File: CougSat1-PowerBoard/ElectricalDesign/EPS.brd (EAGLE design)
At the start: 90.4 x 95.8 mm, 416 parts, among them J1 Deployable 0, J2 PV0, J3 PV1, J4 Umbilical, J5 CougSat Card, J6 SWD, J7 PV2, J8 PV3, J9 Deployable 1, Q1 CSD25402Q3A, Q2 DMN2008LFU, Q3 DMN2008LFU, Q4 CSD25402Q3A, Q5 CSD25402Q3A, Q6 DMN53D0LDW, Q7 DMN53D0LDW, Q8 CSD25402Q3A, SW1 ESE24MH1, U1 INA199C1, U10 INA199C2, U11 INA199C1, U12 AD7689, U13 INA199C2, U14 TPS2115A, U15 TXS0102DQM, U16 TXS0102DQM, U17 AD8515, U18 BQ29700, U19 TPS2115A, U2 AD7689, U20 TXS0102DQM, U21 TXS0102DQM, U22 STM32L476RGT, U23 AD7291, U24 TPS2115A, U25 TPS2115A, U26 BQ29700, U27 TPS2115A, U28 TPS2115A, U29 TPS2115A, U3 AD8515, U30 TPS2115A, U31 INA199C1, U32 TPS2115A, U33 TPS2115A, U34 INA199C1, U35 AD7291, U36 TPS2115A, U37 AD7689, U38 TPS2115A, U39 AD7291, U4 TPS2115A, U40 AD8515, U41 TPS2115A, U42 TPS2115A, U43 TPS2115A, U44 INA199C1, U45 TPS2115A, U46 TPS2115A, U47 TPS64200, U48 TPS2115A, U49 TPS2115A, U5 AD7291, U50 AD7291, U51 TPS2115A, U52 TPS2115A, U53 TPS2115A, U54 TPS2115A, U55 TPS2115A, U6 INA199C1, U7 TPS2115A, U8 TXS0102DQM, U9 TPS64200, Y1 8MHz ±10ppm, Y2 32.768kHz ±10ppm

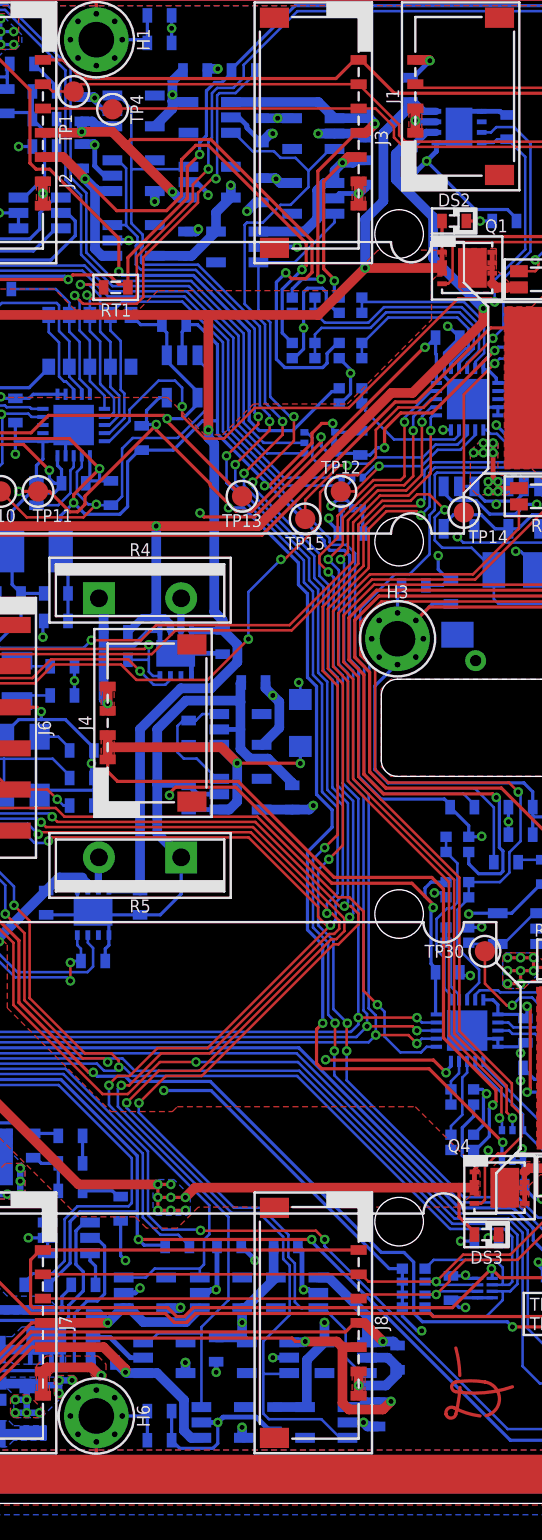
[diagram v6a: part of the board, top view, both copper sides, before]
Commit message: Updated block diagram
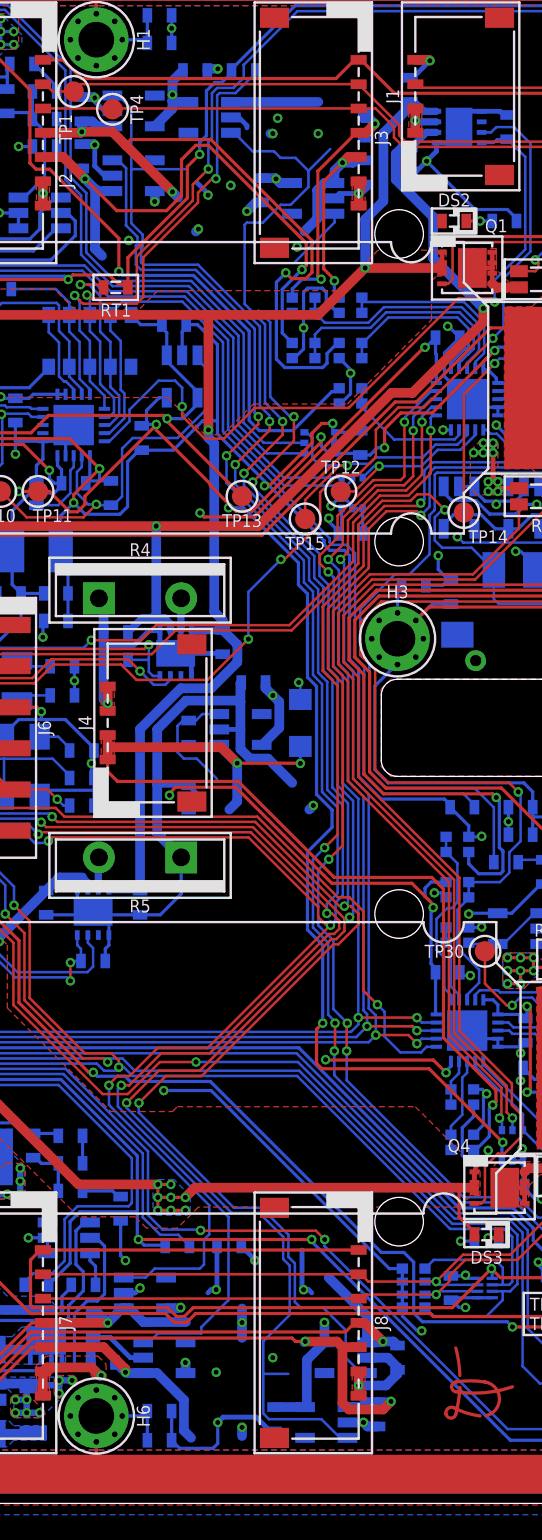
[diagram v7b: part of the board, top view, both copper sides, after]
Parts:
- removed C112, C125, C19, C29, C60: 1µF 10%, CougsInSpace-Capacitors:1608
- removed D10, D15, D16, D19, D2, D21, D4, D7, D8: MAX40200, CougsInSpace-DiscreteSemi:SOT23-5
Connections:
- removed net VIN-A: C117.1, C134.1, C30.1, C6.1, C67.1, D1.5, D11.5, D13.1, D17.5, D20.5, D22.5, D23.5, D3.5, D5.5, D9.5, R2.2
- new net VBATT: DS2.A, Q1.1, Q1.2, Q1.3
- net PC_PV-0/2A: no longer D19.3, D8.3
- net PC_PV-0/2B: no longer D16.3, D2.3
- net PC_PV-1/3A: no longer D21.3, D7.3
- net PC_PV-1/3B: no longer D15.3, D4.3
- net PGND: no longer C112.2, C125.2, C19.2, C29.2, C60.2, D10.2, D15.2, D16.2, D19.2, D2.2, D21.2, D4.2, D7.2, D8.2
- net PV_IN-0A: no longer D19.1
- net PV_IN-0B: no longer D16.1
- net PV_IN-1A: no longer D21.1
- net PV_IN-1B: no longer D15.1
- net PV_IN-2A: no longer D8.1
- net PV_IN-2B: no longer D2.1
- net PV_IN-3A: no longer D7.1
- net PV_IN-3B: no longer D4.1
- net UMB_EN: no longer D10.3
- net UMB_IN: no longer D10.1
- net VBATT-A: no longer DS2.A, Q1.1, Q1.2, Q1.3
- net VIN: now also C117.1, C134.1, C30.1, C6.1, C67.1, D1.5, D11.5, D13.1, D17.5, D20.5, D22.5, D23.5, D3.5, D5.5, D9.5, R2.2
- net VIN-B: no longer C112.1, C125.1, C19.1, C29.1, C60.1, D10.5, D15.5, D16.5, D19.5, D2.5, D21.5, D4.5, D7.5, D8.5
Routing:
- net VIN: track 13.5 -> 159.2 mm, vias 2 -> 19
- net VIN-A: track 145.7 -> 0.00 mm, vias 17 -> 0
- net VIN-B: track 170.7 -> 151.2 mm
- net PGND: track 1160.6 -> 1145.9 mm
- net PC_PV-0/2B: track 128.2 -> 122.9 mm
- net PC_PV-1/3B: track 128.8 -> 123.5 mm
- net VBATT-A: track 315.7 -> 312.5 mm
- net PV_IN-1A: track 23.8 -> 20.6 mm
- net PV_IN-1B: track 20.2 -> 17.4 mm
- net UMB_IN: track 66.5 -> 64.0 mm
- net PC_PV-1/3A: track 132.0 -> 130.3 mm
- net PV_IN-2A: track 38.4 -> 37.2 mm
- net PV_IN-3B: track 55.2 -> 54.2 mm
- net PC_PV-0/2A: track 127.9 -> 127.1 mm
- net VBATT: track 0.00 -> 0.65 mm
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- added copper zone on layer 1, net VIN
- added copper zone on layer 15, net VIN
- added copper zone on layer 16, net VIN
- added copper zone on layer 2, net VIN
- removed copper zone on layer 1, net VIN-A
- removed copper zone on layer 15, net VIN-A
- removed copper zone on layer 16, net VIN-A
- removed copper zone on layer 2, net VIN-A

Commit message: Implement schematic changes
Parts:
- removed C10, C100, C121, C132, C139, C15, C22, C24, C25, C28, C35, C4, C41, C43, C49, C50, C71, C73, C75, C83: 100nF 10%, CougsInSpace-Capacitors:1608
- removed C107, C20: 1µF 10%, CougsInSpace-Capacitors:1608
- removed C11, C26, C3, C31: 10µF 10%, CougsInSpace-Capacitors:3216
- removed C12: 470pF 1%, CougsInSpace-Capacitors:1608
- removed C33: 220µF 10%, CougsInSpace-Capacitors:7132-POL
- removed C34: 4.7pF ±0.1, CougsInSpace-Capacitors:1608
- removed C45: 10µF 10%, CougsInSpace-Capacitors:1608
- removed D12: SS1FH10, CougsInSpace-DiscreteSemi:DO-219AB
- removed D13, D14: MAX40200, CougsInSpace-DiscreteSemi:SOT23-5
- removed D6: MBRM120LT, CougsInSpace-DiscreteSemi:POWERMITE
- removed DS4, DS5: Green, CougsInSpace-LEDs:1608-POL
- removed H5, H6: M2, CougsInSpace-Hardware:MOUNTING_HOLE-2.2
- removed L1: 4.7µH 20%, CougsInSpace-Coils:7575
- removed R36: 10kΩ 0.1%, CougsInSpace-Resistors:1608
- removed RN4: 5kΩ 0.1%, CougsInSpace-Resistors:1616
- removed U52, U53, U54, U55: TPS2115A, CougsInSpace-IC-Power:VSON-8
- added J10: Battery -, CougsInSpace-Connectors:THT-1.5
- added J11: PGND, CougsInSpace-Connectors:THT-1.5
- added J12: Battery +, CougsInSpace-Connectors:THT-1.5
- added J13: VBatt, CougsInSpace-Connectors:THT-1.5
- added Q10, Q12, Q14, Q16, Q17, Q18, Q20, Q21, Q22, Q24, Q26, Q28, Q29, Q30, Q32, Q34, Q35, Q37, Q38, Q40, Q41, Q43, Q9: CSD25402Q3A, CougsInSpace-DiscreteSemi:SON-3333
- added Q11, Q13, Q15, Q19, Q23, Q25, Q27, Q31, Q33, Q36, Q39, Q42: DMN53D0LDW, CougsInSpace-DiscreteSemi:SOT363
- added R84, R86, R88, R90: 12mΩ 1%, CougsInSpace-Resistors:3216-KELVIN
- added R85, R87, R89, R91: 10kΩ 0.1%, CougsInSpace-Resistors:1608
- added RN22, RN23, RN24: 10kΩ 5%, CougsInSpace-Resistors:3264
- added TP44, TP45, TP46, TP47, TP48, TP49, TP50, TP51, TP52, TP53, TP54, TP55, TP56, TP57, TP58, TP59, TP60, TP61, TP62, TP63, TP64: TEST_POINT-SMD-C-1.25, CougsInSpace-Connectors:SMD-C-1.25
- DS1: value Green -> Yellow
- DS3: value Green -> Blue
- Q5: value CSD25402Q3A -> DMN53D0LDW; device CougsInSpace-DiscreteSemi:SON-3333 -> CougsInSpace-DiscreteSemi:SOT363
- Q7: value DMN53D0LDW -> CSD25402Q3A; device CougsInSpace-DiscreteSemi:SOT363 -> CougsInSpace-DiscreteSemi:SON-3333
- R10, R74: value 470Ω 0.5% -> 12mΩ 1%; device CougsInSpace-Resistors:1608 -> CougsInSpace-Resistors:3216-KELVIN
- R11: value 12mΩ 1% -> 10kΩ 0.1%; device CougsInSpace-Resistors:3216-KELVIN -> CougsInSpace-Resistors:1608
- R12, R51, R55, R60, R65, R71, R73, R76, R81: value 2.2kΩ 1% -> 10kΩ 0.1%
- R13: value 150Ω 1% -> 12mΩ 1%; device CougsInSpace-Resistors:1608 -> CougsInSpace-Resistors:3216-KELVIN
- R14: value 10mΩ 1% -> 10kΩ 0.1%; device CougsInSpace-Resistors:3216 -> CougsInSpace-Resistors:1608
- R15, R9: value 0Ω <20mΩ -> 12mΩ 1%; device CougsInSpace-Resistors:1608 -> CougsInSpace-Resistors:3216-KELVIN
- R16, R47, R69: value 1kΩ 0.1% -> 10kΩ 0.1%
- R17: value 1kΩ 0.1% -> 100kΩ 0.1%
- R18: value 360kΩ 1% -> 12mΩ 1%; device CougsInSpace-Resistors:1608 -> CougsInSpace-Resistors:3216-KELVIN
- R19, R21, R23: value 0Ω <20mΩ -> 10kΩ 0.1%
- R20: value 620kΩ 1% -> 12mΩ 1%; device CougsInSpace-Resistors:1608 -> CougsInSpace-Resistors:3216-KELVIN
- R24, R50, R54, R57, R59, R70, R79: value 2.2kΩ 1% -> 12mΩ 1%; device CougsInSpace-Resistors:1608 -> CougsInSpace-Resistors:3216-KELVIN
- R26, R39, R63: value 750Ω 0.5% -> 12mΩ 1%; device CougsInSpace-Resistors:1608 -> CougsInSpace-Resistors:3216-KELVIN
- R38, R45, R58: value 750Ω 0.5% -> 10kΩ 0.1%
- R52: value 10kΩ 0.1% -> 12mΩ 1%; device CougsInSpace-Resistors:1608 -> CougsInSpace-Resistors:3216-KELVIN
- R53: value 536kΩ 1% -> 10kΩ 0.1%
- R56: value 1kΩ 0.1% -> 12mΩ 1%; device CougsInSpace-Resistors:1608 -> CougsInSpace-Resistors:3216-KELVIN
- R67: value 1.2kΩ 0.1% -> 12mΩ 1%; device CougsInSpace-Resistors:1608 -> CougsInSpace-Resistors:3216-KELVIN
- TP37: value TEST_POINT-THT-0.7 -> TEST_POINT-SMD-C-1.25; device CougsInSpace-Connectors:THT-0.7 -> CougsInSpace-Connectors:SMD-C-1.25
- U1, U6: value INA199C1 -> INA199C2
- U14, U19, U24, U25, U27, U28, U29, U30, U32, U33, U36, U38, U4, U41, U42, U43, U45, U46, U48, U49, U51, U7: value TPS2115A -> INA199C2; device CougsInSpace-IC-Power:VSON-8 -> CougsInSpace-IC-Amplifiers:SOT363
- U9: value TPS64200 -> INA199C2; device CougsInSpace-IC-Power:SOT23-6 -> CougsInSpace-IC-Amplifiers:SOT363
- moved DS1 292.1 mm to (-33.2, -245.4)
- moved R81 257.9 mm to (-10.0, -213.6), flipped to the top, turned to 0 degrees
- moved R74 257.0 mm to (-9.20, -202.9), flipped to the top, turned to 0 degrees
- moved R76 254.3 mm to (-12.9, -213.6), flipped to the top, turned to 0 degrees
- moved R79 254.1 mm to (-32.7, -206.8), flipped to the top, turned to 0 degrees
- moved R73 253.9 mm to (-15.8, -213.6), flipped to the top, turned to 0 degrees
- moved R29 238.5 mm to (-33.2, -242.2), flipped to the top, turned to 0 degrees
- moved U51 238.4 mm to (-11.0, -198.9), flipped to the top
- moved R38 234.1 mm to (-27.4, -213.6), flipped to the top, turned to 0 degrees
- moved R55 231.7 mm to (-18.7, -213.6), flipped to the top, turned to 0 degrees
- moved RT5 231.1 mm to (-33.2, -248.6), flipped to the top
- moved R51 228.3 mm to (-21.6, -213.6), flipped to the top, turned to 0 degrees
- moved R69 225.7 mm to (-23.9, -167.8), flipped to the top
- moved R45 224.9 mm to (-24.5, -213.6), flipped to the top, turned to 0 degrees
- moved R56 223.7 mm to (-13.9, -202.9), flipped to the top, turned to 0 degrees
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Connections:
- net 3.3V_I-A renamed 3.3V_I
- net 3.3V_ISENS-A renamed 3.3V_ISENS
- net 3.3V_LED-A renamed 3.3V_LED
- net 3.3V_REG_BUCK_NODE-A renamed 3.3V_REG_BUCK_NODE
- net 3.3V_REG_FB-A renamed 3.3V_REG_FB
- net 3.3V_REG_FBRES_HIGH-A renamed 3.3V_REG_FBRES_HIGH
- net 3.3V_REG_FBRES_LOW-A renamed 3.3V_REG_FBRES_LOW
- net 3.3V_REG_INCAP-A renamed 3.3V_REG_INCAP
- net 3.3V_REG_OUTCAP-A renamed 3.3V_REG_OUTCAP
- net 3.3V_REG_RSENS-A renamed 3.3V_REG_RSENS
- net 3.3V_REG_SNUBBER-A renamed 3.3V_REG_SNUBBER
- net 3.3V_REG_SW-A renamed 3.3V_REG_SW
- net 3.3V_REG_SW_GATE-A renamed 3.3V_REG_SW_GATE
- net I_3.3V_IN-A renamed I_3.3V_IN
- net I_3.3V_IN-A_N renamed I_3.3V_IN_N
- net I_3.3V_IN-A_P renamed I_3.3V_IN_P
- net I_3.3V_OUT-A renamed I_3.3V_OUT
- net I_3.3V_OUT-A_N renamed I_3.3V_OUT_N
- net I_3.3V_OUT-A_P renamed I_3.3V_OUT_P
- net TEMP-REG-A renamed TEMP-REG
- net TEMP-REG-B renamed TEMP-PCB-5
- removed net !PC_DEPLOY-0: U22.9, U52.3
- removed net !PC_DEPLOY-1: U22.25, U4.3
- removed net !VBATT_EN: Q1.4, Q4.4, Q7.2, Q7.3, R52.2
- removed net 3.3V-A: C100.1, C24.1, C41.1, DS1.A, R82.2, RN16.2, U14.8, U36.8, U38.8, U41.8, U42.8, U43.8, U45.8, U46.8, U48.8, U49.8, U51.8, U53.8, U54.8, U55.8, U7.8
- removed net 3.3V-B: C139.1, C28.1, C43.1, DS4.A, R22.1, RN4.2, U14.6, U36.6, U38.6, U41.6, U42.6, U43.6, U45.6, U46.6, U48.6, U49.6, U51.6, U53.6, U54.6, U55.6, U7.6
- removed net 3.3V_I-B: C31.1, C33.A, C34.1, L1.2, R22.2, R23.2, TP36.1
- removed net 3.3V_ISENS-B: Q5.5, Q5.6, Q5.7, Q5.8, Q5.PAD, R14.1, U9.4
- removed net 3.3V_LED-B: DS4.C, R16.2
- removed net 3.3V_REG_BUCK_NODE-B: D6.C, L1.1, Q5.1, Q5.2, Q5.3, R13.2
- removed net 3.3V_REG_FB-B: C34.2, R19.2, R20.1, U9.3
- removed net 3.3V_REG_FBRES_HIGH-B: R20.2, R23.1
- removed net 3.3V_REG_FBRES_LOW-B: R18.2, R19.1
- removed net 3.3V_REG_INCAP-B: C11.2, C3.1
- removed net 3.3V_REG_OUTCAP-B: C26.1, C31.2
- removed net 3.3V_REG_RSENS-B: R11.1, R14.2
- removed net 3.3V_REG_SNUBBER-B: C12.1, R13.1
- removed net 3.3V_REG_SW-B: R15.1, U9.6
- removed net 3.3V_REG_SW_GATE-B: Q5.4, R15.2
- removed net ADC_3.3V-B: RN4.3, RN4.4, U2.6
- removed net EJECT_TIMER_DISCHARGE: Q7.6, R33.1
- removed net I_3.3V: R24.2, U14.4, U23.4
- removed net I_3.3V_IN-B: TP43.1, U1.6, U2.8
- removed net I_3.3V_IN-B_N: R11.1-KELVIN, U1.5
- removed net I_3.3V_IN-B_P: R11.2-KELVIN, U1.4
- removed net I_3.3V_OUT-B: TP42.1, U2.7, U6.6
- removed net I_3.3V_OUT-B_N: R22.1-KELVIN, U6.5
- removed net I_3.3V_OUT-B_P: R22.2-KELVIN, U6.4
- removed net I_DEPLOY-0: R74.2, U35.5, U52.4
- removed net I_DEPLOY-1: R10.2, U4.4, U5.18
- removed net PC_PV-0/2A: D23.3, D9.3, U22.16
- removed net PC_PV-0/2B: D20.3, D5.3, U22.15
- removed net PC_PV-1/3A: D22.3, D3.3, U22.11
- removed net PC_PV-1/3B: D1.3, D17.3, U22.14
- removed net PR_DEPLOY-0: J1.1, J1.2, U52.7
- removed net PR_DEPLOY-1: J9.1, J9.2, U4.7
- removed net PWR_CTRL_SW: J5.A40, J5.B40, R47.1, SW1.1, SW1.2
- removed net UMB_EN: D11.3, R36.1
- removed net VBATT_EN: D12.C, Q7.5, R47.2, R53.1
- removed net VBATT_LED-A: DS2.C, R69.2
- removed net VBATT_LED-B: DS3.C, R17.2
- removed net VIN-B: D14.1, R7.1
- removed net VIN_BATT-A: BT1.C, R1.2, R2.1, R37.2
- removed net VIN_BATT-B: BT2.C, R27.2, R7.2, R8.1
- removed net VIN_OUT-A: Q1.5, Q1.6, Q1.7, Q1.8, Q1.PAD, R1.1
- removed net VIN_OUT-B: Q4.5, Q4.6, Q4.7, Q4.8, Q4.PAD, R8.2
- new net !PC_DP-0: Q39.3, Q40.4, R87.1
- new net !PC_DP-1: Q41.4, Q42.6, R89.1
- new net BATTERY+: J12.1, R1.1, R8.2
- new net BATTERY-: J10.1, Q2.1, Q3.6, R30.1, R31.1, R41.1, R46.1, TP17.1, TP19.1
- new net CHASSIS_REG1: C136.1, H1.1, H1.V1, H1.V2, H1.V3, H1.V4, H1.V5, H1.V6, H1.V7, H1.V8, R83.2
- new net CHASSIS_REG2: C109.1, H2.1, H2.V1, H2.V2, H2.V3, H2.V4, H2.V5, H2.V6, H2.V7, H2.V8, R62.2
- new net I_3.3V-0_N: R9.1-KELVIN, U1.5
- new net I_3.3V-0_P: R9.2-KELVIN, U1.4
- new net I_3.3V-10_N: R63.1-KELVIN, U46.5
- new net I_3.3V-10_P: R63.2-KELVIN, U46.4
- new net I_3.3V-11_N: R67.1-KELVIN, U48.5
- new net I_3.3V-11_P: R67.2-KELVIN, U48.4
- new net I_3.3V-12_N: R70.1-KELVIN, U49.5
- new net I_3.3V-12_P: R70.2-KELVIN, U49.4
- new net I_3.3V-1_N: R13.1-KELVIN, U6.5
- new net I_3.3V-1_P: R13.2-KELVIN, U6.4
- new net I_3.3V-2_N: R15.1-KELVIN, U9.5
- new net I_3.3V-2_P: R15.2-KELVIN, U9.4
- new net I_3.3V-3_N: R18.1-KELVIN, U14.5
- new net I_3.3V-3_P: R18.2-KELVIN, U14.4
- new net I_3.3V-4_N: R20.1-KELVIN, U36.5
- new net I_3.3V-4_P: R20.2-KELVIN, U36.4
- new net I_3.3V-5_N: R22.1-KELVIN, U38.5
- new net I_3.3V-5_P: R22.2-KELVIN, U38.4
- new net I_3.3V-6_N: R24.1-KELVIN, U41.5
- new net I_3.3V-6_P: R24.2-KELVIN, U41.4
- new net I_3.3V-7_N: R52.1-KELVIN, U42.5
- new net I_3.3V-7_P: R52.2-KELVIN, U42.4
- new net I_3.3V-8_N: R57.1-KELVIN, U43.5
- new net I_3.3V-8_P: R57.2-KELVIN, U43.4
- new net I_3.3V-9_N: R59.1-KELVIN, U45.5
- new net I_3.3V-9_P: R59.2-KELVIN, U45.4
- new net I_3.3V-PV_N: R90.1-KELVIN, U51.5
- new net I_3.3V-PV_P: R90.2-KELVIN, U51.4
- new net I_BATT-0_N: R10.1-KELVIN, U4.5
- new net I_BATT-0_P: R10.2-KELVIN, U4.4
- new net I_BATT-1_N: R26.1-KELVIN, U7.5
- new net I_BATT-1_P: R26.2-KELVIN, U7.4
- new net I_BATT-2_N: R39.1-KELVIN, U19.5
- new net I_BATT-2_P: R39.2-KELVIN, U19.4
- new net I_BATT-3_N: R50.1-KELVIN, U24.5
- new net I_BATT-3_P: R50.2-KELVIN, U24.4
- new net I_BATT-4_N: R54.1-KELVIN, U25.5
- new net I_BATT-4_P: R54.2-KELVIN, U25.4
- new net I_BATT-5_N: R56.1-KELVIN, U27.5
- new net I_BATT-5_P: R56.2-KELVIN, U27.4
- new net I_BATT-6_N: R74.1-KELVIN, U28.5
- new net I_BATT-6_P: R74.2-KELVIN, U28.4
- new net I_BH-0_N: R79.1-KELVIN, U29.5
- new net I_BH-0_P: R79.2-KELVIN, U29.4
- new net I_BH-1_N: R84.1-KELVIN, U30.5
- new net I_BH-1_P: R84.2-KELVIN, U30.4
- new net I_DP-0: TP62.1, U32.6, U35.5
- new net I_DP-0_N: R86.1-KELVIN, U32.5
- new net I_DP-0_P: R86.2-KELVIN, U32.4
- new net I_DP-1: TP63.1, U33.6, U5.18
- new net I_DP-1_N: R88.1-KELVIN, U33.5
- new net I_DP-1_P: R88.2-KELVIN, U33.4
- new net PC_3.3V-0: Q5.2, RN22.1, U22.57
- new net PC_3.3V-1: Q5.5, RN22.9, U22.56
- new net PC_3.3V-10: Q27.2, RN23.2, U22.41
- new net PC_3.3V-11: Q27.5, RN23.8, U22.39
- new net PC_3.3V-12: Q31.2, RN23.3, U22.40
- new net PC_3.3V-2: Q11.2, RN22.2, U22.53
- new net PC_3.3V-3: Q11.5, RN22.8, U22.52
- new net PC_3.3V-4: Q15.2, RN22.3, U22.51
- new net PC_3.3V-6: Q19.2, RN22.4, U22.45
- new net PC_3.3V-7: Q19.5, RN22.6, U22.44
- new net PC_3.3V-8: Q23.2, RN23.1, U22.43
- new net PC_3.3V-9: Q23.5, RN23.9, U22.42
- new net PC_3.3V-PV: Q42.5, R29.1, U22.20
- new net PC_BATT-0: Q13.2, RN23.7, U22.38
- new net PC_BATT-1: Q13.5, RN23.4, U22.37
- new net PC_BATT-2: Q25.2, RN23.6, U22.36
- new net PC_BATT-3: Q25.5, RN24.1, U22.35
- new net PC_BATT-4: Q33.2, RN24.9, U22.34
- new net PC_BATT-5: Q33.5, RN24.2, U22.33
- new net PC_BATT-6: Q36.2, RN24.8, U22.61
- new net PC_BH-0: Q36.5, RN24.3, U22.62
- new net PC_BH-1: Q39.2, RN24.7, U22.17
- new net PC_DP-0: Q39.5, RN24.4, U22.9
- new net PC_DP-1: Q42.2, RN24.6, U22.25
- new net PR_DP-0: J1.1, J1.2, Q40.1, Q40.2, Q40.3
- new net PR_DP-1: J9.1, J9.2, Q41.1, Q41.2, Q41.3
- new net PR_FET_3.3V-0: Q4.5, Q4.6, Q4.7, Q4.8, Q4.PAD, R9.1
- new net PR_FET_3.3V-1: Q7.5, Q7.6, Q7.7, Q7.8, Q7.PAD, R13.1
- new net PR_FET_3.3V-10: Q26.5, Q26.6, Q26.7, Q26.8, Q26.PAD, R63.1
- new net PR_FET_3.3V-11: Q28.5, Q28.6, Q28.7, Q28.8, Q28.PAD, R67.1
- new net PR_FET_3.3V-12: Q30.5, Q30.6, Q30.7, Q30.8, Q30.PAD, R70.1
- new net PR_FET_3.3V-2: Q10.5, Q10.6, Q10.7, Q10.8, Q10.PAD, R15.1
- new net PR_FET_3.3V-21: Q40.5, Q40.6, Q40.7, Q40.8, Q40.PAD, R86.1
- new net PR_FET_3.3V-22: Q41.5, Q41.6, Q41.7, Q41.8, Q41.PAD, R88.1
- new net PR_FET_3.3V-3: Q12.5, Q12.6, Q12.7, Q12.8, Q12.PAD, R18.1
- new net PR_FET_3.3V-4: Q14.5, Q14.6, Q14.7, Q14.8, Q14.PAD, R20.1
- new net PR_FET_3.3V-5: Q16.5, Q16.6, Q16.7, Q16.8, Q16.PAD, R22.1
- new net PR_FET_3.3V-6: Q18.5, Q18.6, Q18.7, Q18.8, Q18.PAD, R24.1
- new net PR_FET_3.3V-7: Q20.5, Q20.6, Q20.7, Q20.8, Q20.PAD, R52.1
- new net PR_FET_3.3V-8: Q22.5, Q22.6, Q22.7, Q22.8, Q22.PAD, R57.1
- new net PR_FET_3.3V-9: Q24.5, Q24.6, Q24.7, Q24.8, Q24.PAD, R59.1
- new net PR_FET_3.3V-PV: Q43.5, Q43.6, Q43.7, Q43.8, Q43.PAD, R90.1
- new net PR_FET_BATT-0: Q9.5, Q9.6, Q9.7, Q9.8, Q9.PAD, R10.1
- new net PR_FET_BATT-1: Q17.5, Q17.6, Q17.7, Q17.8, Q17.PAD, R26.1
- new net PR_FET_BATT-2: Q21.5, Q21.6, Q21.7, Q21.8, Q21.PAD, R39.1
- new net PR_FET_BATT-3: Q29.5, Q29.6, Q29.7, Q29.8, Q29.PAD, R50.1
- new net PR_FET_BATT-4: Q32.5, Q32.6, Q32.7, Q32.8, Q32.PAD, R54.1
- new net PR_FET_BATT-5: Q34.5, Q34.6, Q34.7, Q34.8, Q34.PAD, R56.1
- new net PR_FET_BATT-6: Q35.5, Q35.6, Q35.7, Q35.8, Q35.PAD, R74.1
- new net PR_FET_BH-0: Q37.5, Q37.6, Q37.7, Q37.8, Q37.PAD, R79.1
- new net PR_FET_BH-1: Q38.5, Q38.6, Q38.7, Q38.8, Q38.PAD, R84.1
- new net RBF_GATE: Q1.4, R17.1, SW1.C
- new net VBATT_LED: DS2.C, R33.2
- new net VBATT_RBF: J13.1, Q1.5, Q1.6, Q1.7, Q1.8, Q1.PAD, SW1.1, SW1.2
- net !PC_3.3V-0: now also Q4.4, Q5.6, R11.1; no longer U22.57, U55.3
- net !PC_3.3V-1: now also Q5.3, Q7.4, R14.1; no longer U22.56, U54.3
- net !PC_3.3V-10: now also Q26.4, Q27.6, R65.1; no longer U22.41, U41.3
- net !PC_3.3V-11: now also Q27.3, Q28.4, R69.1; no longer U22.39, U38.3
- net !PC_3.3V-12: now also Q30.4, Q31.6, R71.1; no longer U22.40, U36.3
- net !PC_3.3V-2: now also Q10.4, Q11.6, R16.1; no longer U22.53, U53.3
- net !PC_3.3V-3: now also Q11.3, Q12.4, R19.1; no longer U22.52, U51.3
- net !PC_3.3V-4: now also Q14.4, Q15.6, R21.1; no longer U22.51, U49.3
- net !PC_3.3V-5: now also Q15.3, Q16.4, R23.1; no longer Q6.6, U48.3
- net !PC_3.3V-6: now also Q18.4, Q19.6, R47.1; no longer U22.45, U46.3
- net !PC_3.3V-7: now also Q19.3, Q20.4, R53.1; no longer U22.44, U45.3
- net !PC_3.3V-8: now also Q22.4, Q23.6, R58.1; no longer U22.43, U43.3
- net !PC_3.3V-9: now also Q23.3, Q24.4, R60.1; no longer U22.42, U42.3
- net !PC_3.3V-PV: now also Q42.3, Q43.4, R91.1; no longer U22.20, U7.3
- net !PC_BATT-0: now also Q13.6, Q9.4, R12.1; no longer U22.38, U33.3
- net !PC_BATT-1: now also Q13.3, Q17.4, R38.1; no longer U22.37, U32.3
- net !PC_BATT-2: now also Q21.4, Q25.6, R45.1; no longer U22.36, U30.3
- net !PC_BATT-3: now also Q25.3, Q29.4, R51.1; no longer U22.35, U29.3
- net !PC_BATT-4: now also Q32.4, Q33.6, R55.1; no longer U22.34, U28.3
- net !PC_BATT-5: now also Q33.3, Q34.4, R73.1; no longer U22.33, U27.3
- net !PC_BATT-6: now also Q35.4, Q36.6, R76.1; no longer U22.61, U25.3
- net !PC_BH-0: now also Q36.3, Q37.4, R81.1; no longer U22.62, U24.3
- net !PC_BH-1: now also Q38.4, Q39.6, R85.1; no longer U19.3, U22.17
- net 3.3V: now also DS1.A, R11.2, R13.2, R14.2, R15.2, R16.2, R18.2, R19.2, R20.2, R21.2, R22.2, R23.2, R24.2, R47.2, R52.2, R53.2, R57.2, R58.2, R59.2, R60.2, R63.2, R65.2, R67.2, R69.2, R70.2, R71.2, R82.2, R9.2, R90.2, R91.2, RN16.2; no longer C45.1, U14.7
- net AGND: now also U14.1, U14.2, U19.1, U19.2, U2.6, U2.7, U2.8, U23.4, U24.1, U24.2, U25.1, U25.2, U27.1, U27.2, U28.1, U28.2, U29.1, U29.2, U30.1, U30.2, U32.1, U32.2, U33.1, U33.2, U36.1, U36.2, U38.1, U38.2, U4.1, U4.2, U41.1, U41.2, U42.1, U42.2, U43.1, U43.2, U45.1, U45.2, U46.1, U46.2, U48.1, U48.2, U49.1, U49.2, U51.1, U51.2, U7.1, U7.2, U9.1, U9.2; no longer C107.2, C20.2, C25.2, C4.2, Q7.1, RN4.1
- net AVDD: now also U14.3, U19.3, U24.3, U25.3, U27.3, U28.3, U29.3, U30.3, U32.3, U33.3, U36.3, U38.3, U4.3, U41.3, U42.3, U43.3, U45.3, U46.3, U48.3, U49.3, U51.3, U7.3, U9.3; no longer C25.1, C4.1
- net AVREF-0: no longer C107.1
- net AVREF-1: no longer C20.1
- net CHASSIS: no longer C10.1, C109.1, C136.1, C35.1, H1.1, H1.V1, H1.V2, H1.V3, H1.V4, H1.V5, H1.V6, H1.V7, H1.V8, H2.1, H2.V1, H2.V2, H2.V3, H2.V4, H2.V5, H2.V6, H2.V7, H2.V8, H5.1, H5.V1, H5.V2, H5.V3, H5.V4, H5.V5, H5.V6, H5.V7, H5.V8, H6.1, H6.V1, H6.V2, H6.V3, H6.V4, H6.V5, H6.V6, H6.V7, H6.V8, R21.2, R62.2, R83.2, R9.2
- net DGND: no longer Q6.1, R29.1
- net EJECT_TIMER: no longer R33.2
- net I_3.3V-0: now also TP37.1, U1.6; no longer R81.2, U55.4
- net I_3.3V-1: now also TP36.1, U6.6; no longer R79.2, U54.4
- net I_3.3V-10: now also TP50.1, U46.6; no longer R59.2, U41.4
- net I_3.3V-11: now also TP51.1, U48.6; no longer R58.2, U38.4
- net I_3.3V-12: now also TP52.1, U49.6; no longer R57.2, U36.4
- net I_3.3V-2: now also TP42.1, U9.6; no longer R76.2, U53.4
- net I_3.3V-3: now also TP43.1, U14.6; no longer R73.2, U51.4
- net I_3.3V-4: now also TP44.1, U36.6; no longer R71.2, U49.4
- net I_3.3V-5: now also TP45.1, U38.6; no longer R70.2, U48.4
- net I_3.3V-6: now also TP46.1, U41.6; no longer R67.2, U46.4
- net I_3.3V-7: now also TP47.1, U42.6; no longer R65.2, U45.4
- net I_3.3V-8: now also TP48.1, U43.6; no longer R63.2, U43.4
- net I_3.3V-9: now also TP49.1, U45.6; no longer R60.2, U42.4
- net I_3.3V-PV: now also TP64.1, U51.6; no longer R12.2, U7.4
- net I_BATT-0: now also TP53.1, U4.6; no longer R56.2, U33.4
- net I_BATT-1: now also TP54.1, U7.6; no longer R55.2, U32.4
- net I_BATT-2: now also TP55.1, U19.6; no longer R54.2, U30.4
- net I_BATT-3: now also TP56.1, U24.6; no longer R51.2, U29.4
- net I_BATT-4: now also TP57.1, U25.6; no longer R50.2, U28.4
- net I_BATT-5: now also TP58.1, U27.6; no longer R45.2, U27.4
- net I_BATT-6: now also TP59.1, U28.6; no longer R39.2, U25.4
- net I_BH-0: now also TP60.1, U29.6; no longer R38.2, U24.4
- net I_BH-1: now also TP61.1, U30.6; no longer R26.2, U19.4
- net PC_3.3V-5: now also Q15.5, RN22.7; no longer Q6.2, R29.2
- net PGND: now also J11.1, Q11.1, Q11.4, Q13.1, Q13.4, Q15.1, Q15.4, Q19.1, Q19.4, Q23.1, Q23.4, Q25.1, Q25.4, Q27.1, Q27.4, Q31.1, Q33.1, Q33.4, Q36.1, Q36.4, Q39.1, Q39.4, Q42.1, Q42.4, Q5.1, Q5.4, R17.2, R29.2, R33.1, RN22.10, RN22.5, RN23.10, RN23.5, RN24.10, RN24.5; no longer C10.2, C100.2, C12.2, C121.2, C132.2, C139.2, C15.2, C22.2, C24.2, C26.2, C28.2, C3.2, C33.C, C35.2, C41.2, C43.2, C45.2, C49.2, C50.2, C71.2, C73.2, C75.2, C83.2, D13.2, D13.3, D14.2, D14.3, D6.A, Q2.1, Q3.6, Q7.4, R10.1, R12.1, R16.1, R17.1, R18.1, R21.1, R24.1, R26.1, R30.1, R31.1, R38.1, R39.1, R41.1, R45.1, R46.1, R50.1, R51.1, R54.1, R55.1, R56.1, R57.1, R58.1, R59.1, R60.1, R63.1, R65.1, R67.1, R69.1, R70.1, R71.1, R73.1, R74.1, R76.1, R79.1, R81.1, R9.1, SW1.C, TP17.1, TP19.1, TP37.1, U14.1, U14.3, U14.5, U14.PAD, U19.1, U19.5, U19.PAD, U24.1, U24.5, U24.PAD, U25.1, U25.5, U25.PAD, U27.1, U27.5, U27.PAD, U28.1, U28.5, U28.PAD, U29.1, U29.5, U29.PAD, U30.1, U30.5, U30.PAD, U32.1, U32.5, U32.PAD, U33.1, U33.5, U33.PAD, U36.1, U36.5, U36.PAD, U38.1, U38.5, U38.PAD, U4.1, U4.5, U4.PAD, U41.1, U41.5, U41.PAD, U42.1, U42.5, U42.PAD, U43.1, U43.5, U43.PAD, U45.1, U45.5, U45.PAD, U46.1, U46.5, U46.PAD, U48.1, U48.5, U48.PAD, U49.1, U49.5, U49.PAD, U51.1, U51.5, U51.PAD, U52.1, U52.5, U52.PAD, U53.1, U53.5, U53.PAD, U54.1, U54.5, U54.PAD, U55.1, U55.5, U55.PAD, U7.1, U7.5, U7.PAD, U9.1, U9.2
- net PMIC_LED-A: now also DS3.A; no longer DS5.A
- net PMIC_LED-C: now also DS3.C; no longer DS5.C
- net PR_3.3V-0: now also Q4.1, Q4.2, Q4.3; no longer U55.7
- net PR_3.3V-1: now also Q7.1, Q7.2, Q7.3; no longer U54.7
- net PR_3.3V-10: now also Q26.1, Q26.2, Q26.3; no longer U41.7
- net PR_3.3V-11: now also Q28.1, Q28.2, Q28.3; no longer U38.7
- net PR_3.3V-12: now also Q30.1, Q30.2, Q30.3; no longer U36.7
- net PR_3.3V-2: now also Q10.1, Q10.2, Q10.3; no longer U53.7
- net PR_3.3V-3: now also Q12.1, Q12.2, Q12.3; no longer U51.7
- net PR_3.3V-4: now also Q14.1, Q14.2, Q14.3; no longer U49.7
- net PR_3.3V-5: now also Q16.1, Q16.2, Q16.3; no longer U48.7
- net PR_3.3V-6: now also Q18.1, Q18.2, Q18.3; no longer U46.7
- net PR_3.3V-7: now also Q20.1, Q20.2, Q20.3; no longer U45.7
- net PR_3.3V-8: now also Q22.1, Q22.2, Q22.3; no longer U43.7
- net PR_3.3V-9: now also Q24.1, Q24.2, Q24.3; no longer U42.7
- net PR_3.3V-PV: now also Q43.1, Q43.2, Q43.3; no longer U7.7
- net PR_BATT-0: now also Q9.1, Q9.2, Q9.3; no longer U33.7
- net PR_BATT-1: now also Q17.1, Q17.2, Q17.3; no longer U32.7
- net PR_BATT-2: now also Q21.1, Q21.2, Q21.3; no longer U30.7
- net PR_BATT-3: now also Q29.1, Q29.2, Q29.3; no longer U29.7
- net PR_BATT-4: now also Q32.1, Q32.2, Q32.3; no longer U28.7
- net PR_BATT-5: now also Q34.1, Q34.2, Q34.3; no longer U27.7
- net PR_BATT-6: now also Q35.1, Q35.2, Q35.3; no longer U25.7
- net PR_BH-0: now also Q37.1, Q37.2, Q37.3; no longer U24.7
- net PR_BH-1: now also Q38.1, Q38.2, Q38.3; no longer U19.7
- net UMB_IN: no longer D12.A, R36.2
- net VBATT: now also C105.1, R10.2, R12.2, R26.2, R38.2, R39.2, R45.2, R50.2, R51.2, R54.2, R55.2, R56.2, R61.2, R73.2, R74.2, R76.2, R79.2, R81.2, R84.2, R85.2, R86.2, R87.2, R88.2, R89.2, U47.5
- net VBATT-A: now also BT1.C, R1.2, R2.1, R37.2; no longer C105.1, C132.1, C15.1, C49.1, C71.1, C75.1, R61.2, U19.8, U24.8, U25.8, U27.8, U28.8, U29.8, U30.8, U32.8, U33.8, U4.8, U47.5, U52.8
- net VBATT-B: now also BT2.C, R27.2, R7.2, R8.1; no longer C11.1, C121.1, C22.1, C50.1, C73.1, C83.1, DS3.A, Q4.1, Q4.2, Q4.3, R11.2, U19.6, U24.6, U25.6, U27.6, U28.6, U29.6, U30.6, U32.6, U33.6, U4.6, U52.6, U9.5
- net VIN: now also R7.1; no longer D13.1, D13.5, D14.5, R52.1, R53.2
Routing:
- net PGND: track 1145.9 -> 832.2 mm, vias 136 -> 122
- net 3.3V-A: track 304.2 -> 0.00 mm, vias 28 -> 0
- net 3.3V: track 424.0 -> 713.2 mm, vias 29 -> 57
- net 3.3V-B: track 238.4 -> 0.00 mm, vias 35 -> 0
- net VBATT-B: track 331.7 -> 125.3 mm, vias 29 -> 4
- net VIN-B: track 151.2 -> 0.00 mm, vias 14 -> 0
- net VBATT-A: track 312.5 -> 167.7 mm, vias 17 -> 2
- net PC_PV-1/3A: track 130.3 -> 0.00 mm, vias 5 -> 0
- net PC_PV-0/2A: track 127.1 -> 0.00 mm, vias 5 -> 0
- net PC_PV-1/3B: track 123.5 -> 0.00 mm, vias 5 -> 0
- net PC_PV-0/2B: track 122.9 -> 0.00 mm, vias 5 -> 0
- net VIN_BATT-B: track 118.3 -> 0.00 mm, vias 3 -> 0
- net PWR_CTRL_SW: track 115.4 -> 0.00 mm, vias 3 -> 0
- net VIN_BATT-A: track 95.6 -> 0.00 mm, vias 1 -> 0
- net !VBATT_EN: track 92.3 -> 0.00 mm, vias 1 -> 0
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- added copper zone on layer 1, net 3.3V
- added copper zone on layer 16, net 3.3V
- added copper zone on layer 2, net 3.3V
- added copper zone on layer 1, net PR_DP-0
- added copper zone on layer 1, net PR_DP-1
- removed copper zone on layer 1, net 3.3V-A
- removed copper zone on layer 15, net 3.3V-A
- removed copper zone on layer 16, net 3.3V-A
- removed copper zone on layer 2, net 3.3V-A
- removed copper zone on layer 1, net PR_DEPLOY-0
- removed copper zone on layer 1, net PR_DEPLOY-1
- removed copper zone on layer 1, net VIN_BATT-A
- removed copper zone on layer 1, net VIN_BATT-B
